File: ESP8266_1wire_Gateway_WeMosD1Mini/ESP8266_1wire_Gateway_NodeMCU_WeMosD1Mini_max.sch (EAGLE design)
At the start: 56 parts, among them IC1 7805, IC2 5V, IC3 DS2482-100S, IC4 DS18B20, M1 WEMOS, Q1 BSS84, Q2 BSS138, Q3 BSS138, Q4 BSS138

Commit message: v1.2
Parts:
- R18: value cur.limit -> cur.limit (50-100)
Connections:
- net GND: now also LED1.C; no longer LED1.A
- net N$4: now also LED1.A; no longer LED1.C
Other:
- moved on the sheet: LED1
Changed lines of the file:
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@@
 <setting verticaltext="up"/>
 </settings>
-<grid distance="50" unitdist="mil" unit="mil" style="lines" multiple="1" display="no" altdistance="0.01" altunitdist="inch" altunit="inch"/>
+<grid distance="25" unitdist="mil" unit="mil" style="lines" multiple="1" display="no" altdistance="0.01" altunitdist="inch" altunit="inch"/>
 <layers>
 <layer number="1" name="Top" color="4" fill="1" visible="no" active="no"/>
@@
 <part name="GND5" library="supply1" deviceset="GND" device=""/>
 <part name="Q1" library="transistor-small-signal" deviceset="BSS84" device=""/>
-<part name="R18" library="my" deviceset="R0805_SMALL_GAP" device="" value="cur.limit"/>
+<part name="R18" library="my" deviceset="R0805_SMALL_GAP" device="" value="cur.limit (50-100)"/>
 <part name="R17" library="my" deviceset="R0805_SMALL_GAP" device="" value="100*"/>
 <part name="Q2" library="my" deviceset="BSS138" device=""/>
@@
 </instance>
 <instance part="R19" gate="G$1" x="147.32" y="100.965"/>
-<instance part="LED1" gate="G$1" x="159.385" y="100.965" smashed="yes" rot="R270">
-<attribute name="NAME" x="159.258" y="103.759" size="1.778" layer="95"/>
+<instance part="LED1" gate="G$1" x="159.385" y="100.965" smashed="yes" rot="R90">
+<attribute name="NAME" x="167.132" y="105.791" size="1.778" layer="95" rot="R180"/>
 </instance>
 <instance part="GND3" gate="1" x="169.545" y="100.965" rot="R90"/>
@@
 </segment>
 <segment>
-<wire x1="161.925" y1="100.965" x2="167.005" y2="100.965" width="0.1524" layer="91"/>
-<pinref part="LED1" gate="G$1" pin="A"/>
-<pinref part="GND3" gate="1" pin="GND"/>
-</segment>
-<segment>
 <pinref part="OPT" gate="G$1" pin="2"/>
 <pinref part="GND2" gate="1" pin="GND"/>
@@
 <wire x1="121.285" y1="123.825" x2="109.855" y2="123.825" width="0.1524" layer="91"/>
 <junction x="121.285" y="123.825"/>
+</segment>
+<segment>
+<pinref part="GND3" gate="1" pin="GND"/>
+<pinref part="LED1" gate="G$1" pin="C"/>
+<wire x1="167.005" y1="100.965" x2="164.465" y2="100.965" width="0.1524" layer="91"/>
 </segment>
 </net>
@@
 </segment>
 </net>
-<net name="N$4" class="0">
-<segment>
-<pinref part="R19" gate="G$1" pin="2"/>
-<wire x1="152.4" y1="100.965" x2="154.305" y2="100.965" width="0.1524" layer="91"/>
-<pinref part="LED1" gate="G$1" pin="C"/>
-</segment>
-</net>
 <net name="N$11" class="0">
 <segment>
@@
 </segment>
 </net>
+<net name="N$4" class="0">
+<segment>
+<pinref part="R19" gate="G$1" pin="2"/>
+<wire x1="152.4" y1="100.965" x2="156.845" y2="100.965" width="0.1524" layer="91"/>
+<pinref part="LED1" gate="G$1" pin="A"/>
+</segment>
+</net>

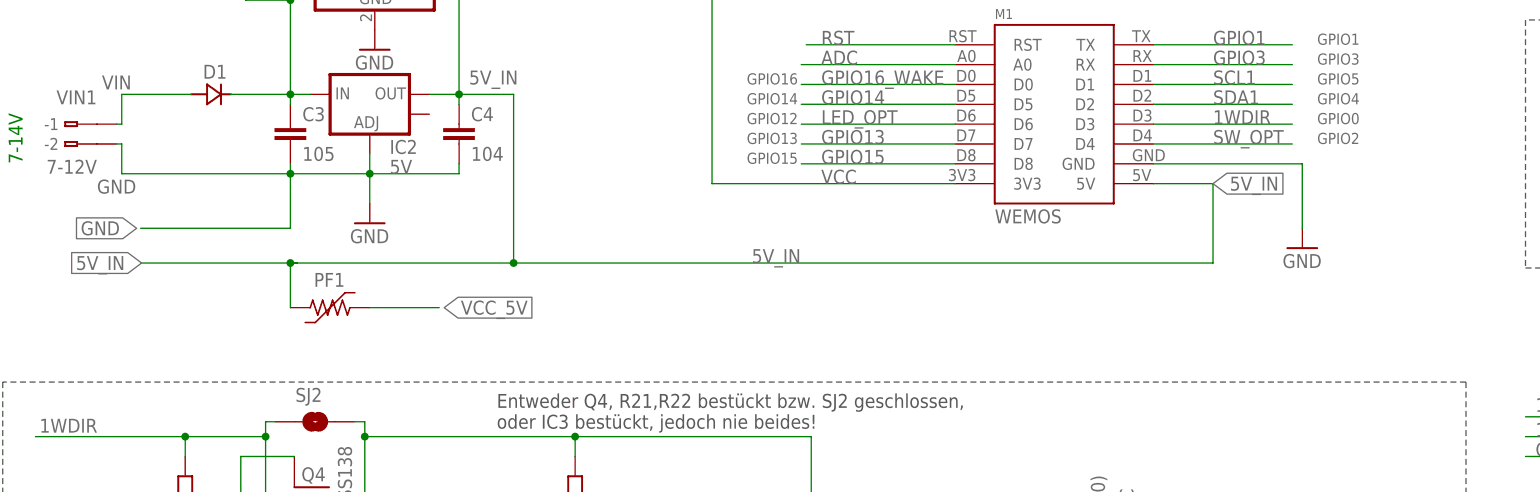
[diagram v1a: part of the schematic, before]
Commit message: v1.3 (new diode to protect ams1117 by power over usb)
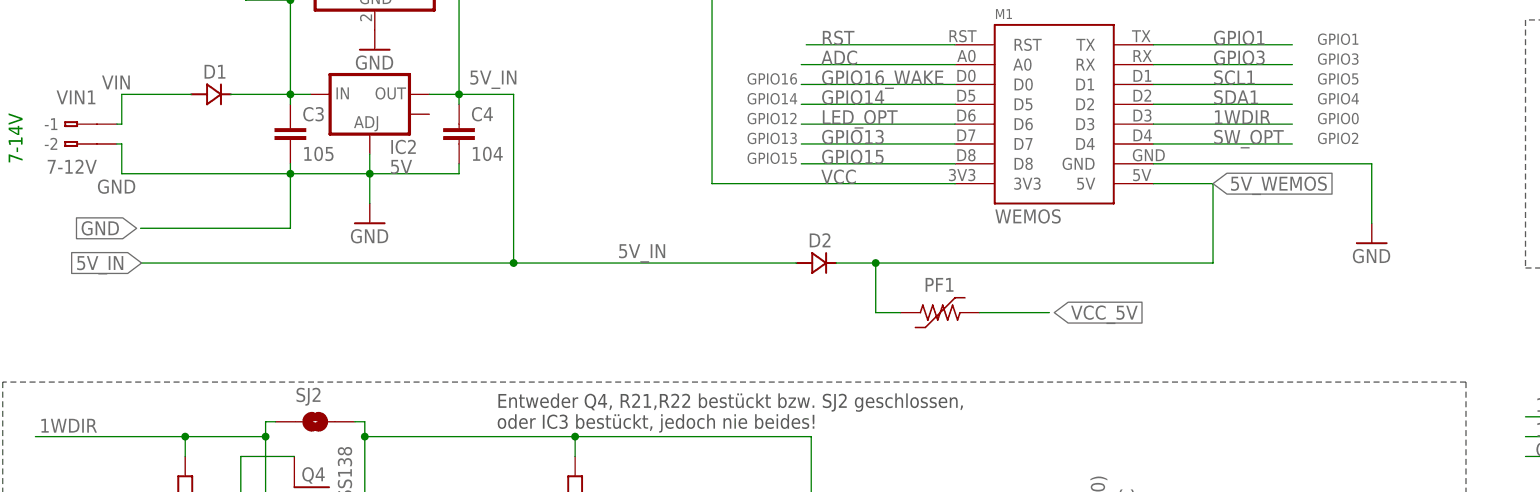
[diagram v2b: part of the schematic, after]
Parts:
- added D2: SS14, ihpcb-diode:SS14
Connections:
- new net 5V_WEMOS: D2.CATHODE, M1.5V, PF1.2
- net 5V_IN: now also D2.ANODE; no longer M1.5V, PF1.2
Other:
- moved on the sheet: PF1
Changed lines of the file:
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@@
 <part name="SJ4" library="SparkFun-Passives" deviceset="JUMPER-PAD-3-NO" device="YES_SILK" value="direct | busmaster"/>
 <part name="JP1" library="my" deviceset="PINHD-1X3_S" device=""/>
+<part name="D2" library="ihpcb-diode" deviceset="SS14" device="" value="SS14"/>
 </parts>
 <sheets>
@@
 <instance part="C3" gate="G$1" x="-38.1" y="96.52"/>
 <instance part="C4" gate="G$1" x="-16.51" y="96.52"/>
-<instance part="PF1" gate="G$1" x="-33.02" y="73.025" smashed="yes" rot="R180">
-<attribute name="NAME" x="-31.115" y="77.47" size="1.778" layer="95" rot="R180"/>
+<instance part="PF1" gate="G$1" x="45.085" y="72.39" smashed="yes" rot="R180">
+<attribute name="NAME" x="46.99" y="76.835" size="1.778" layer="95" rot="R180"/>
 </instance>
 <instance part="VIN1" gate="G$1" x="-67.945" y="96.52" rot="MR0"/>
@@
 </instance>
 <instance part="M1" gate="G$1" x="52.07" y="86.36"/>
-<instance part="GND10" gate="1" x="91.44" y="80.645"/>
+<instance part="GND10" gate="1" x="100.33" y="81.28"/>
 <instance part="IC1" gate="A1" x="-27.305" y="116.205"/>
 <instance part="GND9" gate="1" x="-27.305" y="106.045"/>
@@
 </instance>
 <instance part="JP1" gate="A" x="40.64" y="18.415"/>
+<instance part="D2" gate="D" x="29.21" y="78.74" smashed="yes">
+<attribute name="NAME" x="28.1686" y="80.7466" size="1.778" layer="95"/>
+</instance>
 </instances>
 <busses>
@@
 </segment>
 <segment>
-<wire x1="72.39" y1="91.44" x2="91.44" y2="91.44" width="0.1524" layer="91"/>
+<wire x1="72.39" y1="91.44" x2="100.33" y2="91.44" width="0.1524" layer="91"/>
 <pinref part="M1" gate="G$1" pin="GND"/>
-<wire x1="91.44" y1="91.44" x2="91.44" y2="83.185" width="0.1524" layer="91"/>
+<wire x1="100.33" y1="91.44" x2="100.33" y2="83.82" width="0.1524" layer="91"/>
 <pinref part="GND10" gate="1" pin="GND"/>
 </segment>
@@
 <net name="5V_IN" class="0">
 <segment>
-<wire x1="72.39" y1="88.9" x2="80.01" y2="88.9" width="0.1524" layer="91"/>
-<pinref part="M1" gate="G$1" pin="5V"/>
-<label x="80.01" y="88.9" size="1.778" layer="95" xref="yes"/>
 <pinref part="C4" gate="G$1" pin="1"/>
 <wire x1="-16.51" y1="100.33" x2="-9.525" y2="100.33" width="0.1524" layer="91"/>
@@
 <label x="-15.24" y="101.6" size="1.778" layer="95"/>
 <wire x1="-9.525" y1="100.33" x2="-9.525" y2="78.74" width="0.1524" layer="91"/>
-<wire x1="-9.525" y1="78.74" x2="-38.1" y2="78.74" width="0.1524" layer="91"/>
-<wire x1="-38.1" y1="78.74" x2="-38.1" y2="73.025" width="0.1524" layer="91"/>
-<wire x1="-37.211" y1="78.74" x2="-38.1" y2="78.74" width="0.1524" layer="91"/>
-<junction x="-38.1" y="78.74"/>
-<wire x1="-38.1" y1="78.74" x2="-57.277" y2="78.74" width="0.1524" layer="91"/>
+<wire x1="-9.525" y1="78.74" x2="-57.277" y2="78.74" width="0.1524" layer="91"/>
 <label x="-57.15" y="78.74" size="1.778" layer="95" rot="R180" xref="yes"/>
-<pinref part="PF1" gate="G$1" pin="2"/>
-<label x="20.955" y="78.74" size="1.778" layer="95"/>
-<wire x1="-9.525" y1="78.74" x2="80.01" y2="78.74" width="0.1524" layer="91"/>
+<label x="3.81" y="79.375" size="1.778" layer="95"/>
+<wire x1="-9.525" y1="78.74" x2="26.67" y2="78.74" width="0.1524" layer="91"/>
 <junction x="-9.525" y="78.74"/>
-<wire x1="80.01" y1="88.9" x2="80.01" y2="78.74" width="0.1524" layer="91"/>
 <pinref part="IC1" gate="A1" pin="VO"/>
 <wire x1="-17.145" y1="116.205" x2="-16.51" y2="116.205" width="0.1524" layer="91"/>
@@
 <wire x1="-16.51" y1="127" x2="-16.51" y2="116.205" width="0.1524" layer="91"/>
 <junction x="-16.51" y="116.205"/>
+<pinref part="D2" gate="D" pin="ANODE"/>
 </segment>
 </net>
@@
 <segment>
 <pinref part="PF1" gate="G$1" pin="1"/>
-<wire x1="-27.94" y1="73.025" x2="-19.05" y2="73.025" width="0.1524" layer="91"/>
-<label x="-18.415" y="73.025" size="1.778" layer="95" xref="yes"/>
+<wire x1="50.165" y1="72.39" x2="59.055" y2="72.39" width="0.1524" layer="91"/>
+<label x="59.69" y="72.39" size="1.778" layer="95" xref="yes"/>
 </segment>
 <segment>
@@
 </segment>
 </net>
+<net name="5V_WEMOS" class="0">
+<segment>
+<pinref part="M1" gate="G$1" pin="5V"/>
+<wire x1="72.39" y1="88.9" x2="80.01" y2="88.9" width="0.1524" layer="91"/>
+<wire x1="80.01" y1="88.9" x2="80.01" y2="78.74" width="0.1524" layer="91"/>
+<wire x1="31.75" y1="78.74" x2="36.83" y2="78.74" width="0.1524" layer="91"/>
+<pinref part="D2" gate="D" pin="CATHODE"/>
+<label x="80.01" y="88.9" size="1.778" layer="95" xref="yes"/>
+<pinref part="PF1" gate="G$1" pin="2"/>
+<wire x1="36.83" y1="78.74" x2="80.01" y2="78.74" width="0.1524" layer="91"/>
+<wire x1="36.83" y1="78.74" x2="36.83" y2="72.39" width="0.1524" layer="91"/>
+<wire x1="36.83" y1="72.39" x2="40.005" y2="72.39" width="0.1524" layer="91"/>
+<junction x="36.83" y="78.74"/>
+</segment>
+</net>

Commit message: Schutzdiode + Korrekturen
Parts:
- added R5: 470, resistor:R-EU_R0805
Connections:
- net GPIO16_WAKE: now also R5.2
- net N$8: no longer SJ1.1
- net RST: now also R5.1
- net VIN: now also SJ1.1
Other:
- moved on the sheet: SJ1
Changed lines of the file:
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@@
 <layer number="112" name="tSilk" color="7" fill="1" visible="yes" active="yes"/>
 <layer number="113" name="IDFDebug" color="7" fill="1" visible="yes" active="yes"/>
+<layer number="114" name="FRNTMAAT1" color="7" fill="1" visible="yes" active="yes"/>
+<layer number="115" name="FRNTMAAT2" color="7" fill="1" visible="yes" active="yes"/>
 <layer number="116" name="Patch_BOT" color="9" fill="4" visible="yes" active="yes"/>
+<layer number="117" name="BACKMAAT1" color="7" fill="1" visible="yes" active="yes"/>
+<layer number="118" name="Rect_Pads" color="7" fill="1" visible="no" active="no"/>
+<layer number="119" name="KAP_TEKEN" color="7" fill="1" visible="yes" active="yes"/>
+<layer number="120" name="KAP_MAAT1" color="7" fill="1" visible="yes" active="yes"/>
 <layer number="121" name="_tsilk" color="7" fill="1" visible="yes" active="yes"/>
 <layer number="122" name="_bsilk" color="7" fill="1" visible="yes" active="yes"/>
@@
 <layer number="128" name="_bValues" color="7" fill="1" visible="yes" active="yes"/>
 <layer number="129" name="Mask" color="7" fill="1" visible="yes" active="yes"/>
+<layer number="130" name="SMDSTROOK" color="7" fill="1" visible="yes" active="yes"/>
 <layer number="131" name="tAdjust" color="7" fill="1" visible="yes" active="yes"/>
 <layer number="132" name="bAdjust" color="7" fill="1" visible="yes" active="yes"/>
@@
 <layer number="230" name="230bmp" color="7" fill="1" visible="yes" active="yes"/>
 <layer number="231" name="231bmp" color="7" fill="1" visible="yes" active="yes"/>
+<layer number="232" name="Eagle3D_PG2" color="7" fill="1" visible="yes" active="yes"/>
+<layer number="233" name="Eagle3D_PG3" color="7" fill="1" visible="yes" active="yes"/>
 <layer number="248" name="Housing" color="7" fill="1" visible="yes" active="yes"/>
 <layer number="249" name="Edge" color="7" fill="1" visible="yes" active="yes"/>
@@
 <part name="JP1" library="my" deviceset="PINHD-1X3_S" device=""/>
 <part name="D2" library="ihpcb-diode" deviceset="SS14" device="" value="SS14"/>
+<part name="R5" library="resistor" deviceset="R-EU_" device="R0805" value="470"/>
 </parts>
 <sheets>
@@
 <instance part="IC1" gate="A1" x="-27.305" y="116.205"/>
 <instance part="GND9" gate="1" x="-27.305" y="106.045"/>
-<instance part="SJ1" gate="G$1" x="-43.815" y="119.38" smashed="yes" rot="R90">
-<attribute name="NAME" x="-46.355" y="116.84" size="1.778" layer="95" rot="R90"/>
+<instance part="SJ1" gate="G$1" x="-49.53" y="120.015" smashed="yes" rot="R90">
+<attribute name="NAME" x="-52.07" y="117.475" size="1.778" layer="95" rot="R90"/>
 </instance>
 <instance part="SJ2" gate="G$1" x="-34.925" y="58.42" smashed="yes">
@@
 <attribute name="NAME" x="28.1686" y="80.7466" size="1.778" layer="95"/>
 </instance>
+<instance part="R5" gate="G$1" x="19.685" y="106.68" rot="R180"/>
 </instances>
 <busses>
@@
 <segment>
 <pinref part="D1" gate="D" pin="ANODE"/>
-<wire x1="-50.8" y1="100.33" x2="-59.69" y2="100.33" width="0.1524" layer="91"/>
+<wire x1="-50.8" y1="100.33" x2="-53.975" y2="100.33" width="0.1524" layer="91"/>
+<wire x1="-53.975" y1="100.33" x2="-59.69" y2="100.33" width="0.1524" layer="91"/>
 <wire x1="-59.69" y1="100.33" x2="-59.69" y2="96.52" width="0.1524" layer="91"/>
 <wire x1="-59.69" y1="96.52" x2="-60.325" y2="96.52" width="0.1524" layer="91"/>
 <label x="-62.23" y="100.965" size="1.778" layer="95"/>
 <pinref part="VIN1" gate="G$1" pin="B-1"/>
+<pinref part="SJ1" gate="G$1" pin="1"/>
+<wire x1="-49.53" y1="114.935" x2="-49.53" y2="112.395" width="0.1524" layer="91"/>
+<wire x1="-49.53" y1="112.395" x2="-53.975" y2="112.395" width="0.1524" layer="91"/>
+<wire x1="-53.975" y1="112.395" x2="-53.975" y2="100.33" width="0.1524" layer="91"/>
+<junction x="-53.975" y="100.33"/>
 </segment>
 </net>
 <net name="GPIO16_WAKE" class="0">
 <segment>
-<wire x1="27.305" y1="101.6" x2="46.99" y2="101.6" width="0.1524" layer="91"/>
 <pinref part="M1" gate="G$1" pin="D0"/>
 <label x="29.845" y="101.6" size="1.778" layer="95"/>
+<wire x1="12.7" y1="101.6" x2="46.99" y2="101.6" width="0.1524" layer="91"/>
+<wire x1="12.7" y1="101.6" x2="12.7" y2="106.68" width="0.1524" layer="91"/>
+<pinref part="R5" gate="G$1" pin="2"/>
+<wire x1="12.7" y1="106.68" x2="14.605" y2="106.68" width="0.1524" layer="91"/>
 </segment>
 </net>
@@
 <pinref part="IC1" gate="A1" pin="VI"/>
 <wire x1="-37.465" y1="116.205" x2="-38.1" y2="116.205" width="0.1524" layer="91"/>
-<wire x1="-38.1" y1="116.205" x2="-38.1" y2="112.395" width="0.1524" layer="91"/>
-<pinref part="SJ1" gate="G$1" pin="1"/>
-<wire x1="-38.1" y1="112.395" x2="-38.1" y2="100.33" width="0.1524" layer="91"/>
-<wire x1="-43.815" y1="114.3" x2="-43.815" y2="112.395" width="0.1524" layer="91"/>
-<wire x1="-43.815" y1="112.395" x2="-38.1" y2="112.395" width="0.1524" layer="91"/>
-<junction x="-38.1" y="112.395"/>
+<wire x1="-38.1" y1="116.205" x2="-38.1" y2="100.33" width="0.1524" layer="91"/>
 </segment>
 </net>
@@
 <wire x1="-16.51" y1="116.205" x2="-16.51" y2="100.33" width="0.1524" layer="91"/>
 <pinref part="SJ1" gate="G$1" pin="2"/>
-<wire x1="-43.815" y1="124.46" x2="-43.815" y2="127" width="0.1524" layer="91"/>
-<wire x1="-43.815" y1="127" x2="-16.51" y2="127" width="0.1524" layer="91"/>
+<wire x1="-49.53" y1="125.095" x2="-49.53" y2="127" width="0.1524" layer="91"/>
+<wire x1="-49.53" y1="127" x2="-16.51" y2="127" width="0.1524" layer="91"/>
 <wire x1="-16.51" y1="127" x2="-16.51" y2="116.205" width="0.1524" layer="91"/>
 <junction x="-16.51" y="116.205"/>
@@
 </segment>
 <segment>
-<wire x1="7.62" y1="125.095" x2="15.875" y2="125.095" width="0.1524" layer="91"/>
-<wire x1="15.875" y1="125.095" x2="86.995" y2="125.095" width="0.1524" layer="91"/>
+<wire x1="7.62" y1="125.095" x2="10.795" y2="125.095" width="0.1524" layer="91"/>
+<wire x1="10.795" y1="125.095" x2="86.995" y2="125.095" width="0.1524" layer="91"/>
 <label x="8.255" y="125.095" size="1.778" layer="95" rot="R180" xref="yes"/>
-<wire x1="15.875" y1="88.9" x2="15.875" y2="125.095" width="0.1524" layer="91"/>
-<junction x="15.875" y="125.095"/>
+<wire x1="10.795" y1="88.9" x2="10.795" y2="125.095" width="0.1524" layer="91"/>
+<junction x="10.795" y="125.095"/>
 <label x="29.845" y="88.9" size="1.778" layer="95"/>
 <pinref part="M1" gate="G$1" pin="3V3"/>
-<wire x1="15.875" y1="88.9" x2="46.99" y2="88.9" width="0.1524" layer="91"/>
+<wire x1="10.795" y1="88.9" x2="46.99" y2="88.9" width="0.1524" layer="91"/>
 </segment>
 <segment>
@@
 </segment>
 <segment>
-<wire x1="46.99" y1="106.68" x2="27.94" y2="106.68" width="0.1524" layer="91"/>
+<wire x1="46.99" y1="106.68" x2="24.765" y2="106.68" width="0.1524" layer="91"/>
 <pinref part="M1" gate="G$1" pin="RST"/>
 <label x="29.845" y="106.68" size="1.778" layer="95"/>
-</segment>
-</net>
+<pinref part="R5" gate="G$1" pin="1"/>
+</segment>
+</net>
